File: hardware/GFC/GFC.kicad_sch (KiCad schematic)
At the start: 24 parts

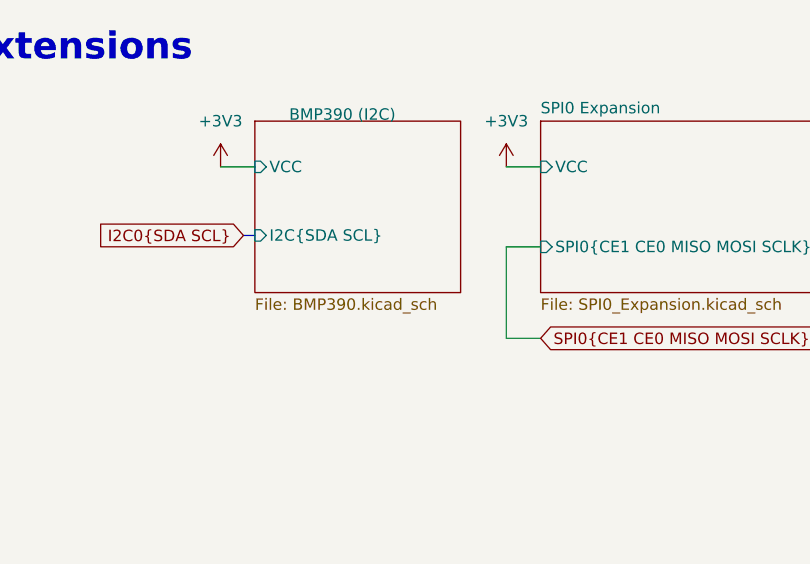
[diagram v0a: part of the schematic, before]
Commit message: Cleaning up the hardware directory
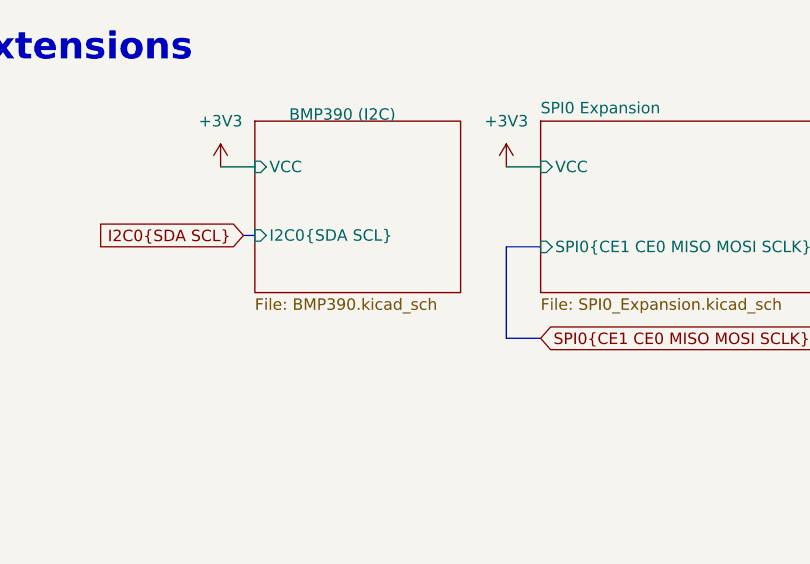
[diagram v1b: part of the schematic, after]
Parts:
- C20: footprint (none) -> Capacitor_SMD:C_0603_1608Metric_Pad1.08x0.95mm_HandSolder
- CPU1: footprint Connector_PinSocket_2.54mm:PinSocket_2x20_P2.54mm_Vertical -> Connector_PinSocket_2.54mm:PinSocket_2x20_P2.54mm_Vertical_SMD
- LED1: footprint (none) -> LED_SMD:LED_0805_2012Metric
- Op_R1, Op_R2, R2: footprint (none) -> Resistor_SMD:R_0603_1608Metric_Pad0.98x0.95mm_HandSolder
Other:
- sheet BMP390 (I2C) ports: added I2C0{SDA SCL}; removed I2C{SDA SCL}

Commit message: PCB Prototype
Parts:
- removed C20: 100nF, Capacitor_SMD:C_0603_1608Metric_Pad1.08x0.95mm_HandSolder, symbol Device:C
- removed CPU1: Pi Zero/Zero W, Connector_PinSocket_2.54mm:PinSocket_2x20_P2.54mm_Vertical_SMD, symbol Connector_Generic:Conn_02x20_Odd_Even
- removed LED1: Status LED, LED_SMD:LED_0805_2012Metric, symbol Device:LED
- removed Op_R1, Op_R2, R2: R, Resistor_SMD:R_0603_1608Metric_Pad0.98x0.95mm_HandSolder, symbol Device:R
- removed R1: 4.7k, Resistor_SMD:R_0603_1608Metric_Pad0.98x0.95mm_HandSolder, symbol Device:R
- removed TP10, TP11, TP12, TP13, TP14, TP15, TP16, TP17, TP18, TP2, TP3, TP4, TP5, TP6, TP7, TP8, TP9: Test Point, TestPoint:TestPoint_Pad_D1.0mm, symbol Connector:TestPoint_Small
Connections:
- no-connect marks 8 -> 0
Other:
- removed sheet 1-Wire Connection
- removed sheet BMP390 (I2C)
- removed sheet DAC
- removed sheet DRA818
- removed sheet EEPROM
- removed sheet Power
- removed sheet SAM-M8Q (I2C)
- removed sheet SPI0 Expansion
- added sheet GFC_HAT (GFC_HAT.kicad_sch)
- added sheet GFC_SHOE (GFC_SHOE.kicad_sch)
- note removed: "GPIO Configuration EEPROM"
- note removed: "Power/Battery Management"
- note removed: "Raspberry Pi Header"
- note removed: "Sensors/Extensions"
- note removed: "USB DAC/ADC"
- note removed: "VHF Radio Module"
